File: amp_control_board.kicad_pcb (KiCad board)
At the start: 2 copper layers, 100.1 x 61 mm, 84 parts, among them J1 Conn_01x03_Male, J2 Conn_01x04_Female, J3 Conn_01x03_Male, J4 Screw_Terminal_01x02, J5 Conn_01x04_Female, J6 Conn_02x03_Odd_Even, J7 Conn_01x03_Male, J8 USB_B_Mini, M1 Fan_4pin, M2 Fan_4pin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

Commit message: finished routing logic
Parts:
- moved R10 2.62 mm to (134.6, 108.6)
- moved R11 2.62 mm to (134.6, 111.8)
- moved R13 2.62 mm to (134.6, 114.9)
- moved J3 2.04 mm to (143.6, 121.8)
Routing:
- net I2C_SCL: track 12.3 -> 135.4 mm, vias 0 -> 2
- net I2C_SDA: track 12.6 -> 135.6 mm, vias 0 -> 2
- net TIM3_CH3: track 9.27 -> 79.4 mm, vias 0 -> 2
- net SWDIO: track 0.00 -> 68.5 mm, vias 0 -> 2
- net SWCLK: track 0.00 -> 65.3 mm, vias 0 -> 2
- net TIM4_CH3: track 0.00 -> 52.7 mm, vias 0 -> 2
- net AUDIO_IN_L: track 27.6 -> 22.6 mm
- net AUDIO_IN_R: track 37.9 -> 34.3 mm
- net SPI_NSS: track 35.5 -> 32.7 mm
- net SPI_SCK: track 35.9 -> 33.1 mm
- net BOOT0: track 23.5 -> 25.9 mm
- net OSCIN: track 23.8 -> 25.3 mm
- net SPI_MOSI: track 36.1 -> 34.6 mm
- net OSCOUT: track 26.9 -> 25.7 mm
- net BTN_MODE: track 38.8 -> 39.9 mm
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
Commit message: 90% routing done
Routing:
- net VDD_3V3: track 142.0 -> 232.8 mm, vias 2 -> 5
- net VDD_5V: track 88.7 -> 171.3 mm
- net USB_M: track 65.1 -> 62.0 mm
- net USB_P: track 64.0 -> 61.0 mm
- net USB_DT: track 59.1 -> 58.0 mm

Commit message: top routing done expect for maybe USB protection
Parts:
- moved D3 6.55 mm to (149.4, 100.2), turned to 270 degrees
- moved R7 3.26 mm to (149.4, 95.1), turned to 270 degrees
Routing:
- net VDD_3V3: track 232.8 -> 346.1 mm, vias 5 -> 9
- net TIM2_CH2: track 62.7 -> 69.2 mm
- net LSE_OSC1: track 20.3 -> 26.7 mm
- net I2C_SDA: track 135.6 -> 130.0 mm
- net I2C_SCL: track 135.4 -> 129.9 mm
- net LSE_OSC2: track 25.1 -> 30.5 mm
- net TIM1_CH1: track 43.0 -> 48.3 mm
- net TIM3_CH3: track 79.5 -> 81.9 mm

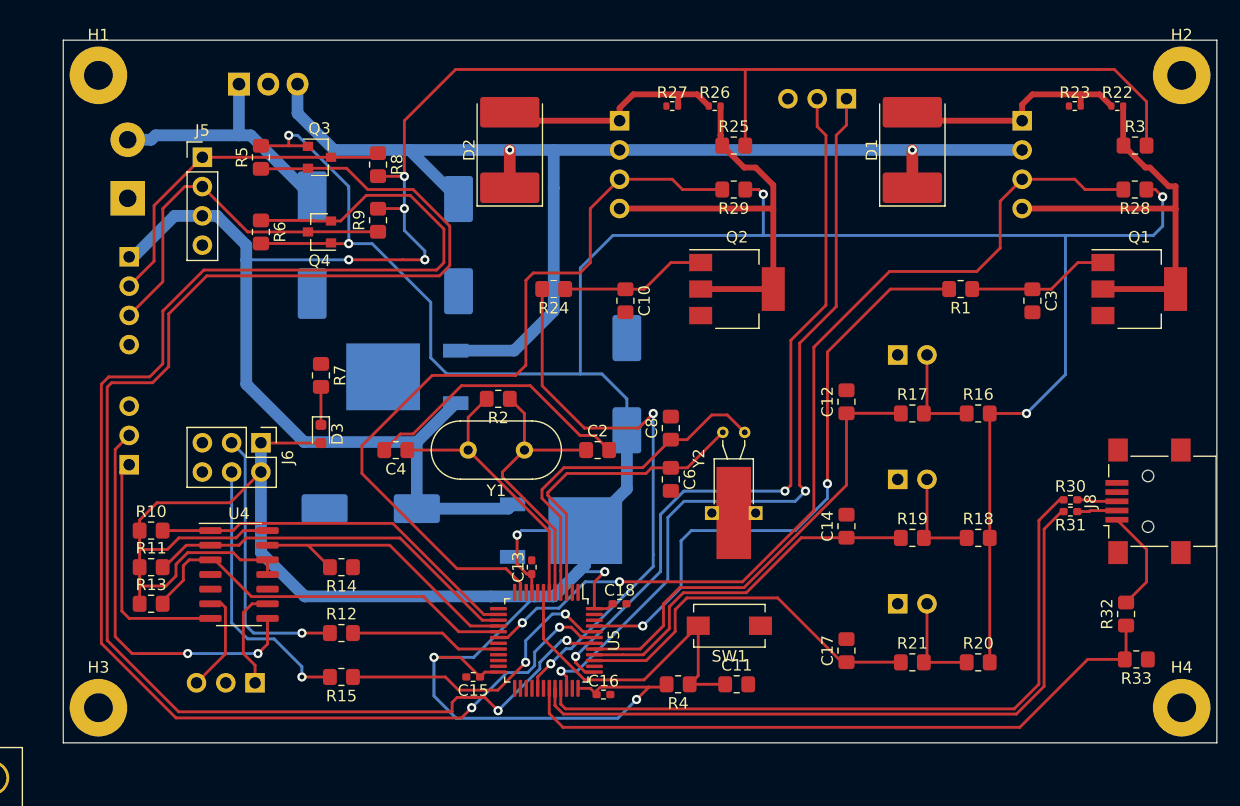
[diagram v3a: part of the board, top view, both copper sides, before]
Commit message: added USB protection
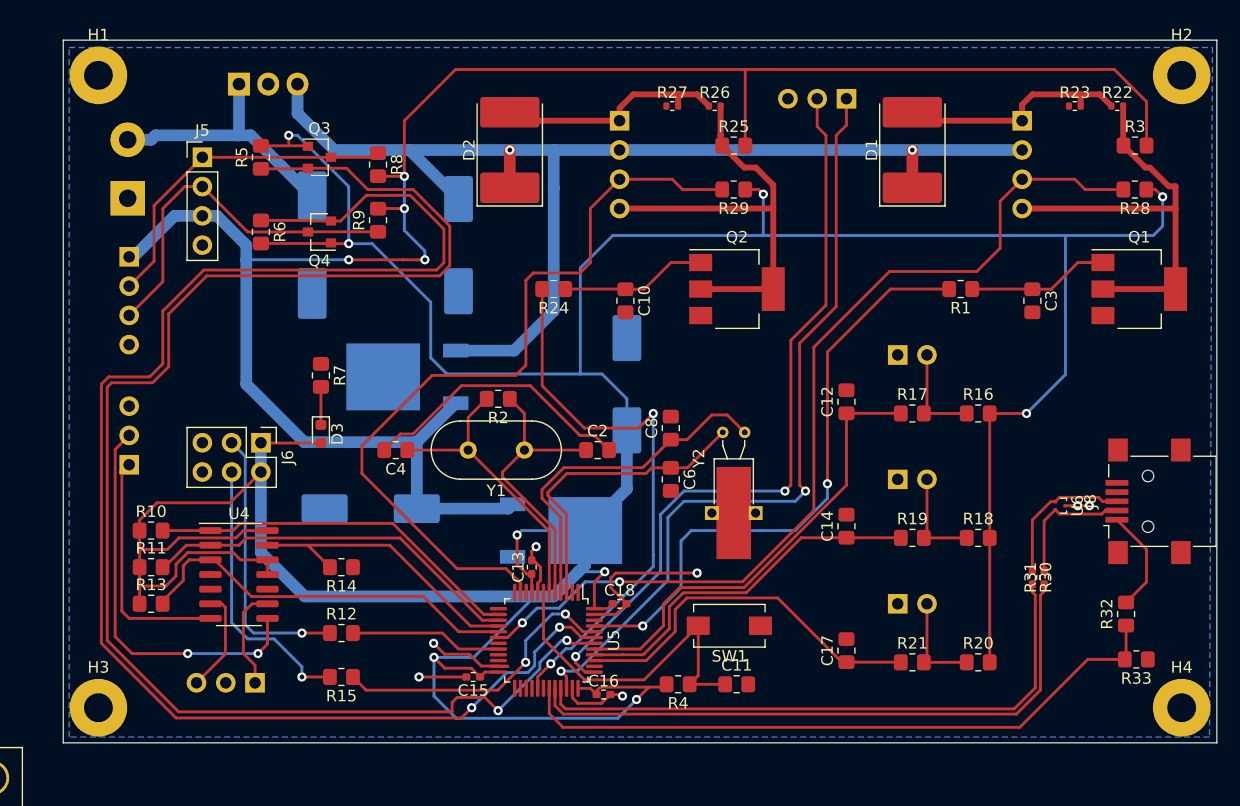
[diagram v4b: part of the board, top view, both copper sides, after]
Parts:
- added U6: TPD2EUSB30, Package_TO_SOT_SMD:Texas_DRT-3, F.Cu at (213.5, 106.4)
- moved R30 7.50 mm to (211.1, 112.6), turned to 270 degrees
- moved R31 6.16 mm to (212.1, 112.6), turned to 90 degrees
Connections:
- R30 pad 1: USB_P -> Net-(J8-Pad3)
- R30 pad 2: Net-(J8-Pad3) -> USB_P
- R31 pad 1: Net-(J8-Pad2) -> USB_M
- R31 pad 2: USB_M -> Net-(J8-Pad2)
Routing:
- net GND: track 0.00 -> 37.5 mm, vias 0 -> 7
- net Net-(J8-Pad3): track 3.49 -> 12.8 mm
- net USB_P: track 61.0 -> 52.5 mm
- net Net-(J8-Pad2): track 3.47 -> 11.4 mm
- net USB_M: track 62.0 -> 54.9 mm
- added copper zone on B.Cu, net GND

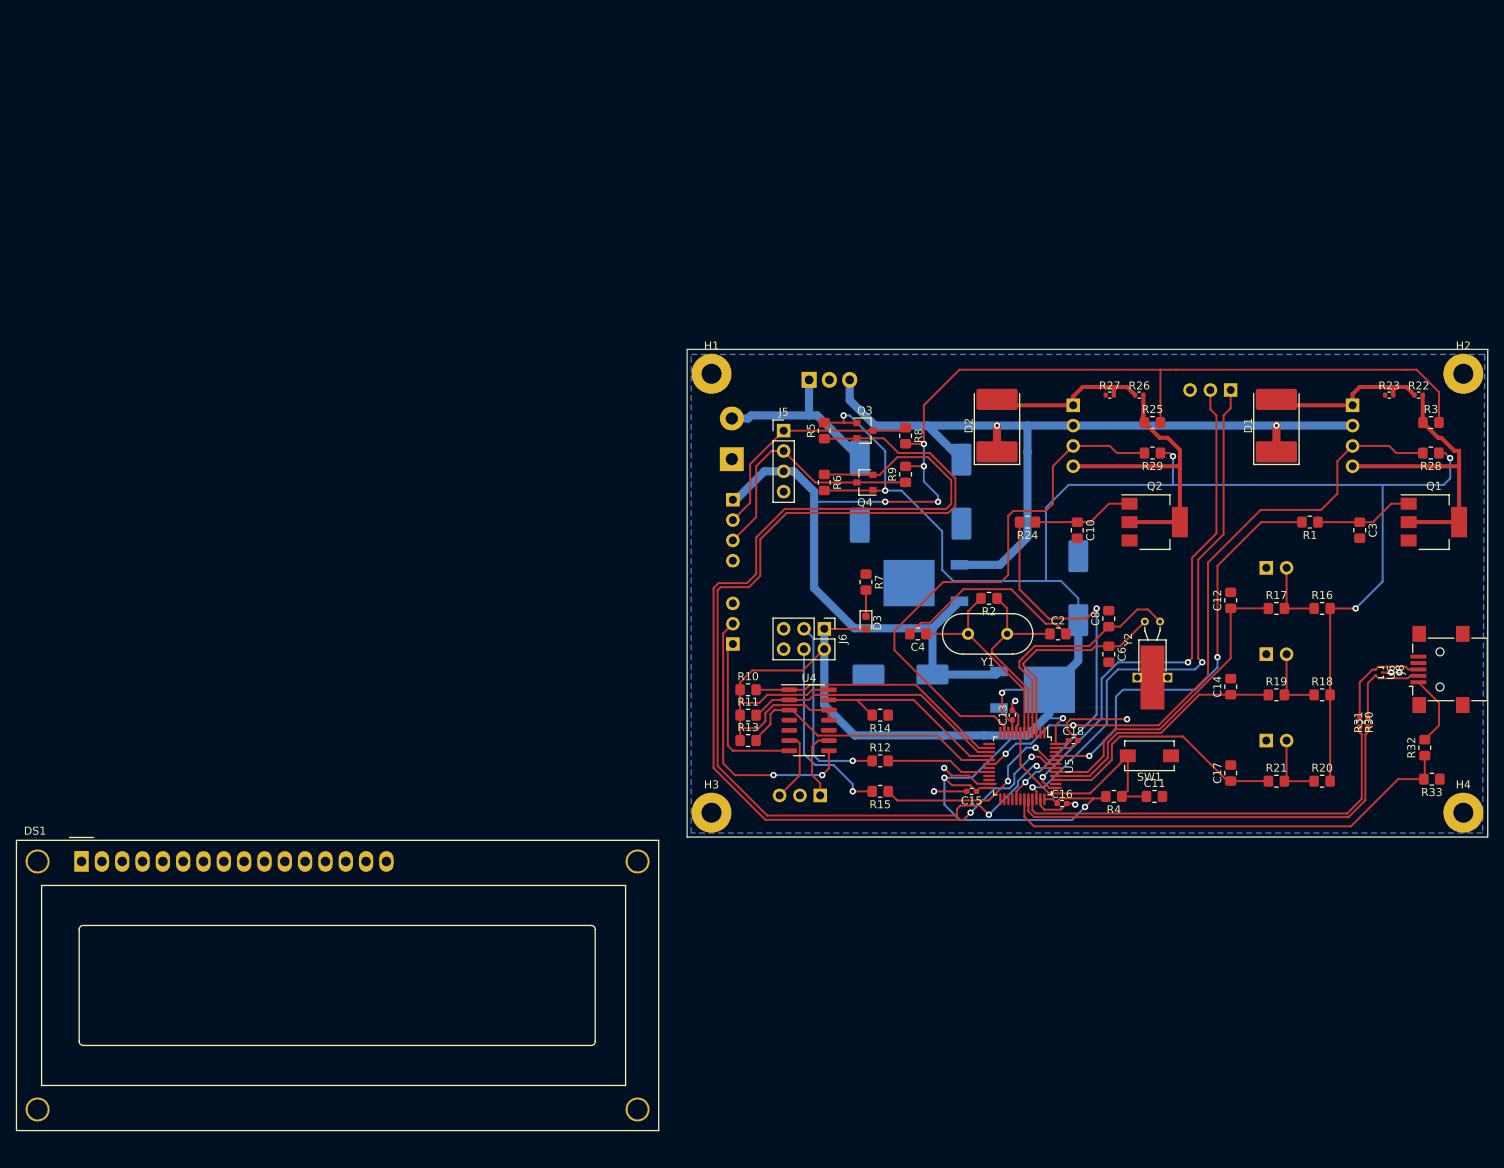
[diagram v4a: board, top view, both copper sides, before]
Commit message: finished routing, need to place stiching vias
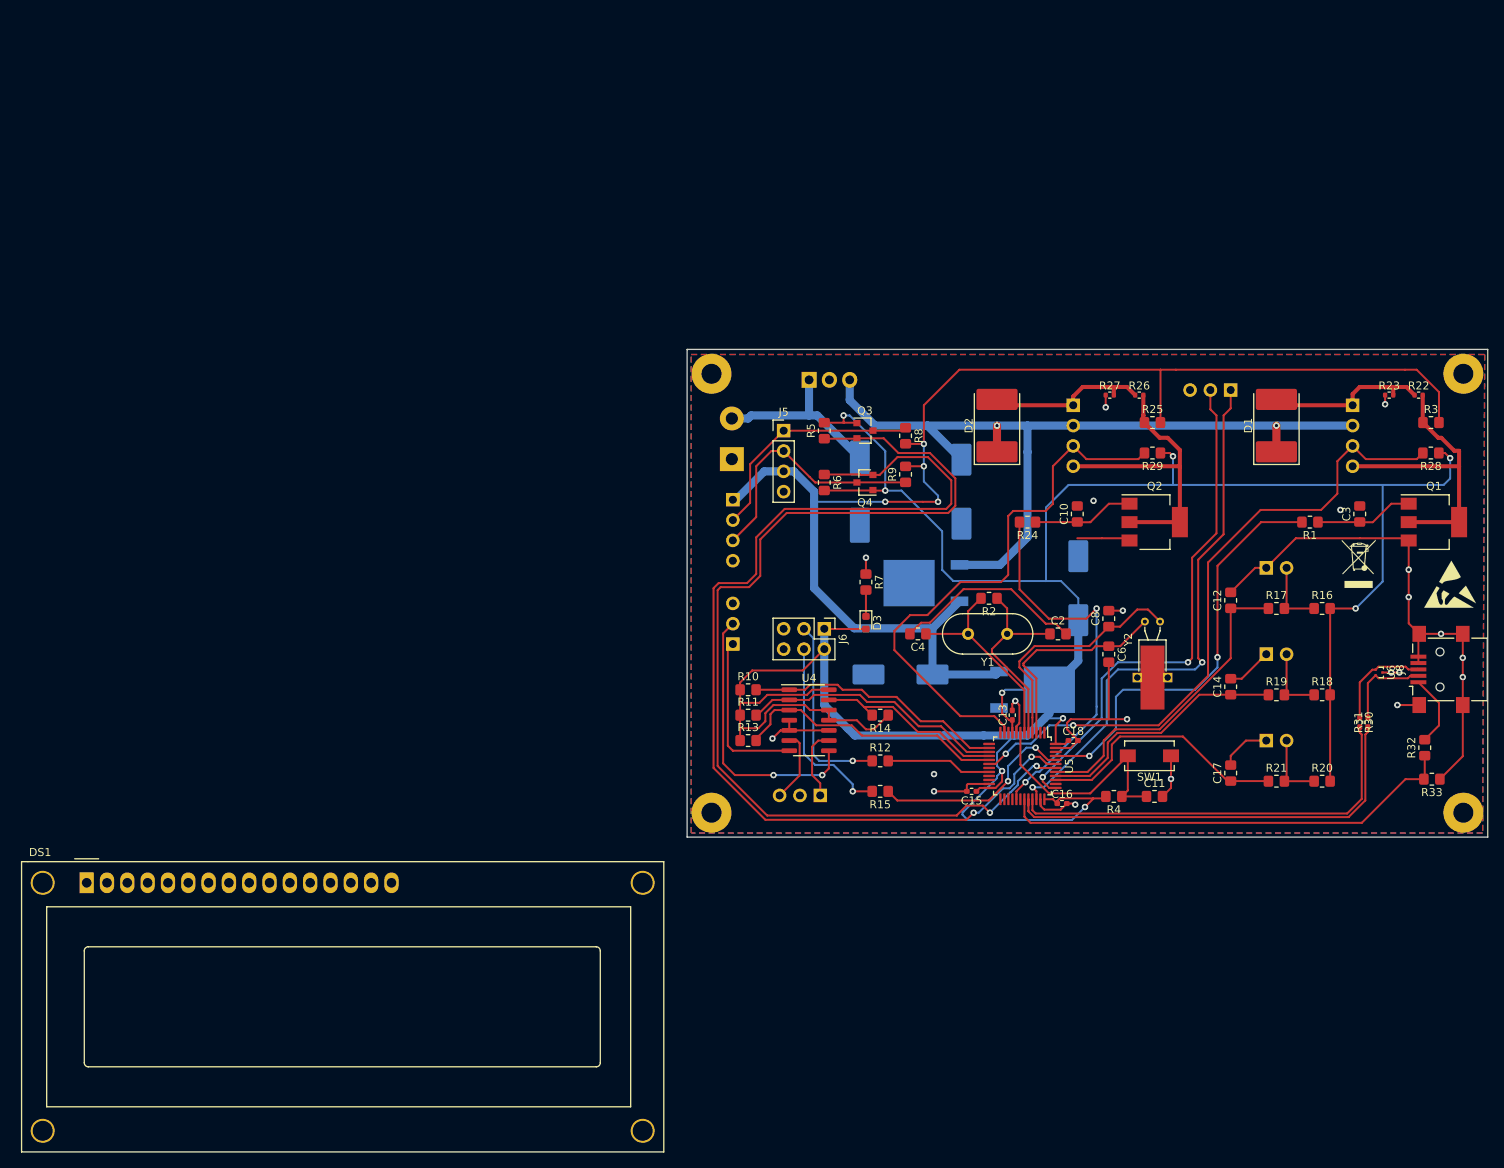
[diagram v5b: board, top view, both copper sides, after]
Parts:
- added REF**: WEEE-Logo_4.2x6mm_SilkScreen, Symbol:WEEE-Logo_4.2x6mm_SilkScreen, F.Cu at (210.9, 92.8)
- added REF**: ESD-Logo_6.6x6mm_SilkScreen, Symbol:ESD-Logo_6.6x6mm_SilkScreen, F.Cu at (222.4, 95.4)
- moved DS1 2.74 mm to (51.9, 132.7)
- moved C10 2.03 mm to (175.8, 86.6), turned to 90 degrees
- moved C3 2.03 mm to (211.1, 86.6), turned to 90 degrees
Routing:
- net GND: track 37.5 -> 150.4 mm, vias 7 -> 21
- net VDD_3V3: track 346.1 -> 349.6 mm
- net SPI_MISO: track 25.6 -> 24.4 mm
- net I2C_SCL: track 129.9 -> 129.2 mm
- net TIM2_CH2: track 69.2 -> 69.8 mm
- net TIM3_CH3: track 81.9 -> 82.4 mm
- added copper zone on F.Cu, net GND

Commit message: silkscreen more or less done.
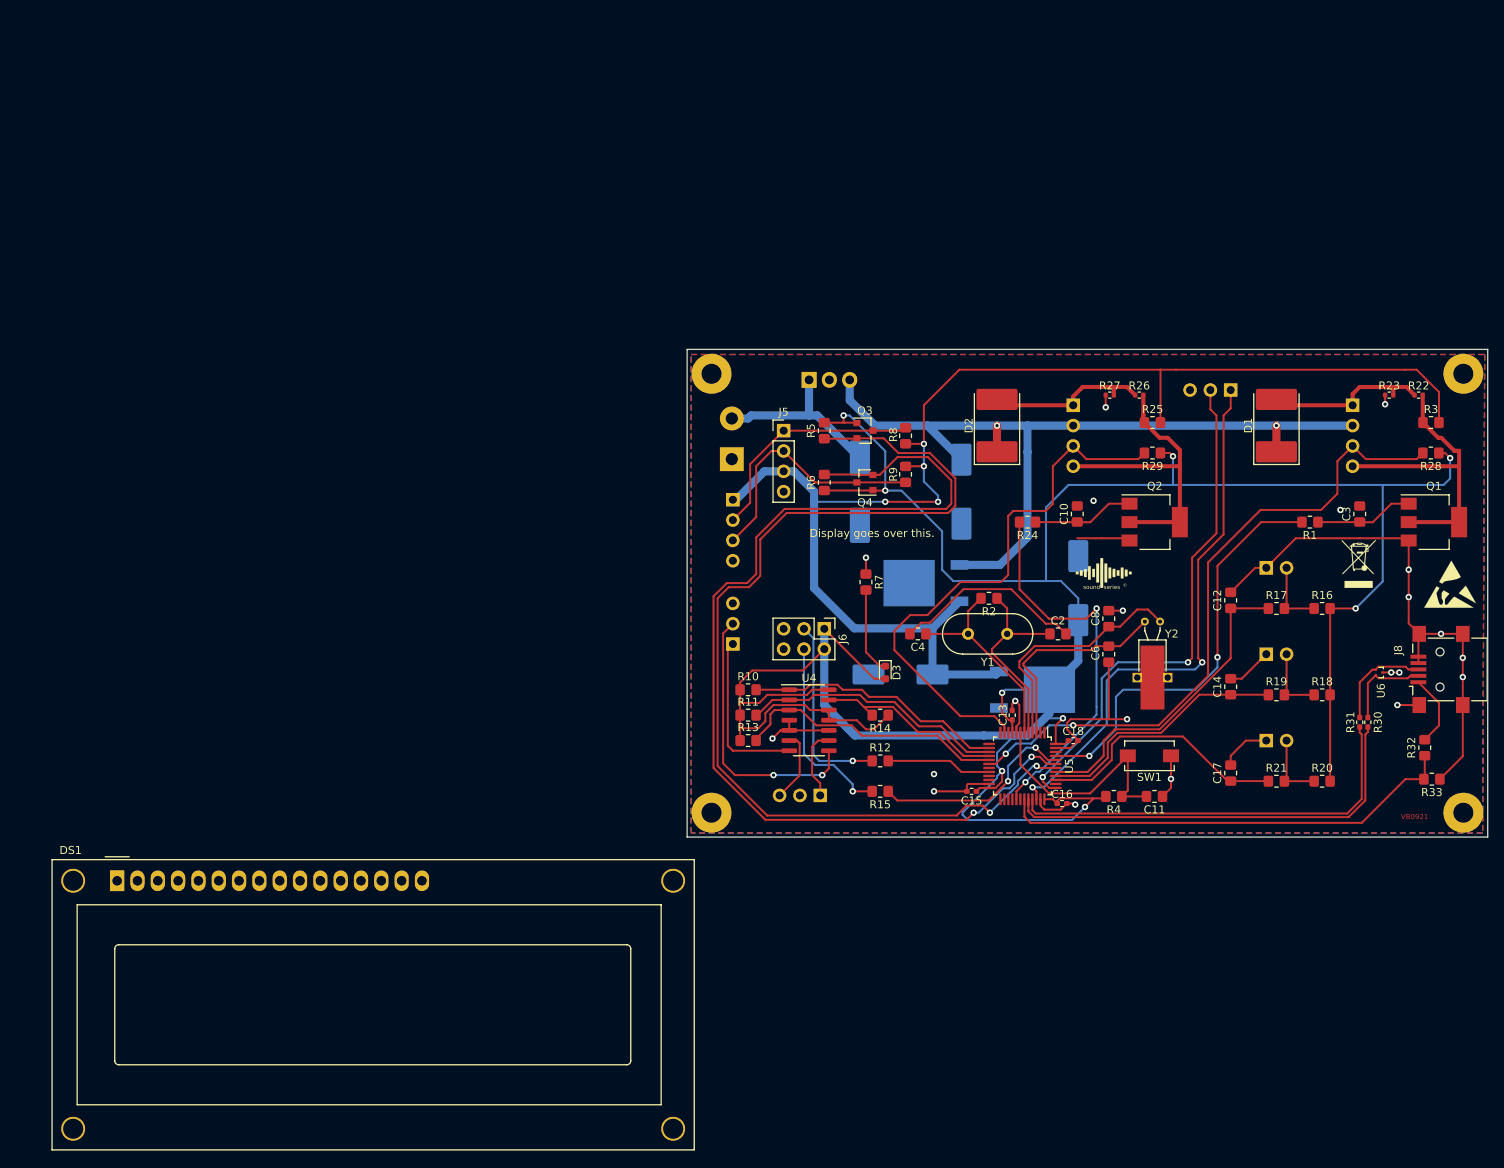
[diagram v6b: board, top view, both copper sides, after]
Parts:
- added G***: LOGO, graphics_own:sound_7x7mm, F.Cu at (179.1, 94.0)
- added G***: LOGO, graphics_own:high_voltage_43x43, B.Cu at (136.3, 69.5)
- added G***: LOGO, graphics_own:silk_graphics_neg_1x1cm, B.Cu at (214.5, 119.9)
- added REF**: OSHW-Symbol_6.7x6mm_SilkScreen, Symbol:OSHW-Symbol_6.7x6mm_SilkScreen, B.Cu at (132.5, 117.2)
- moved D3 6.67 mm to (151.8, 106.4)
- moved DS1 3.82 mm to (55.8, 132.5)
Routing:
- net Net-(D3-Pad1): track 3.29 -> 10.9 mm
- net VDD_3V3: track 349.6 -> 354.6 mm
- net I2C_SDA: track 130.0 -> 129.4 mm
- net I2C_SCL: track 129.2 -> 128.6 mm
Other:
- board text added: "<-Me, the designer."
- board text added: "Amp control board rev.1"
- board text added: "Display goes over this."
- board text added: "VB0921"
- board text added: "sound series"
- board text added: "©"

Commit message: project as sent to production
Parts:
- removed DS1: HY1602E, Display:WC1602A
- moved G*** 1.91 mm to (216.0, 121.0)
- moved G*** 0.80 mm to (137.0, 69.7)
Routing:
- net GND: vias 21 -> 140
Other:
- board text added: "Display area."
- board text added: "Up to 35V!"
- board text removed: "<-Me, the designer."
- board text removed: "Display goes over this."
